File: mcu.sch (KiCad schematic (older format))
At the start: 71 parts, among them J10 JTAG, J11 esp32L, J12 esp32B, J13 esp32R, J2 SPI1, J3 uSD, J4 I2C1, J5 serial1, J6 serial2, J7 touch interface, J8 LCD 4.3, J9 EXT_IOS, Q1 ZXMN2F30FH, Q2 ZXMN2F30FH, Q3 ZXMN2F30FH, SW1 reset, U3 AT25SF641, U5 STM32F750Z8, U6 MP3302DJ-LF-P, U7 ESP32-WROOM-32, Y1 25MHz, Y2 32.768 kHz

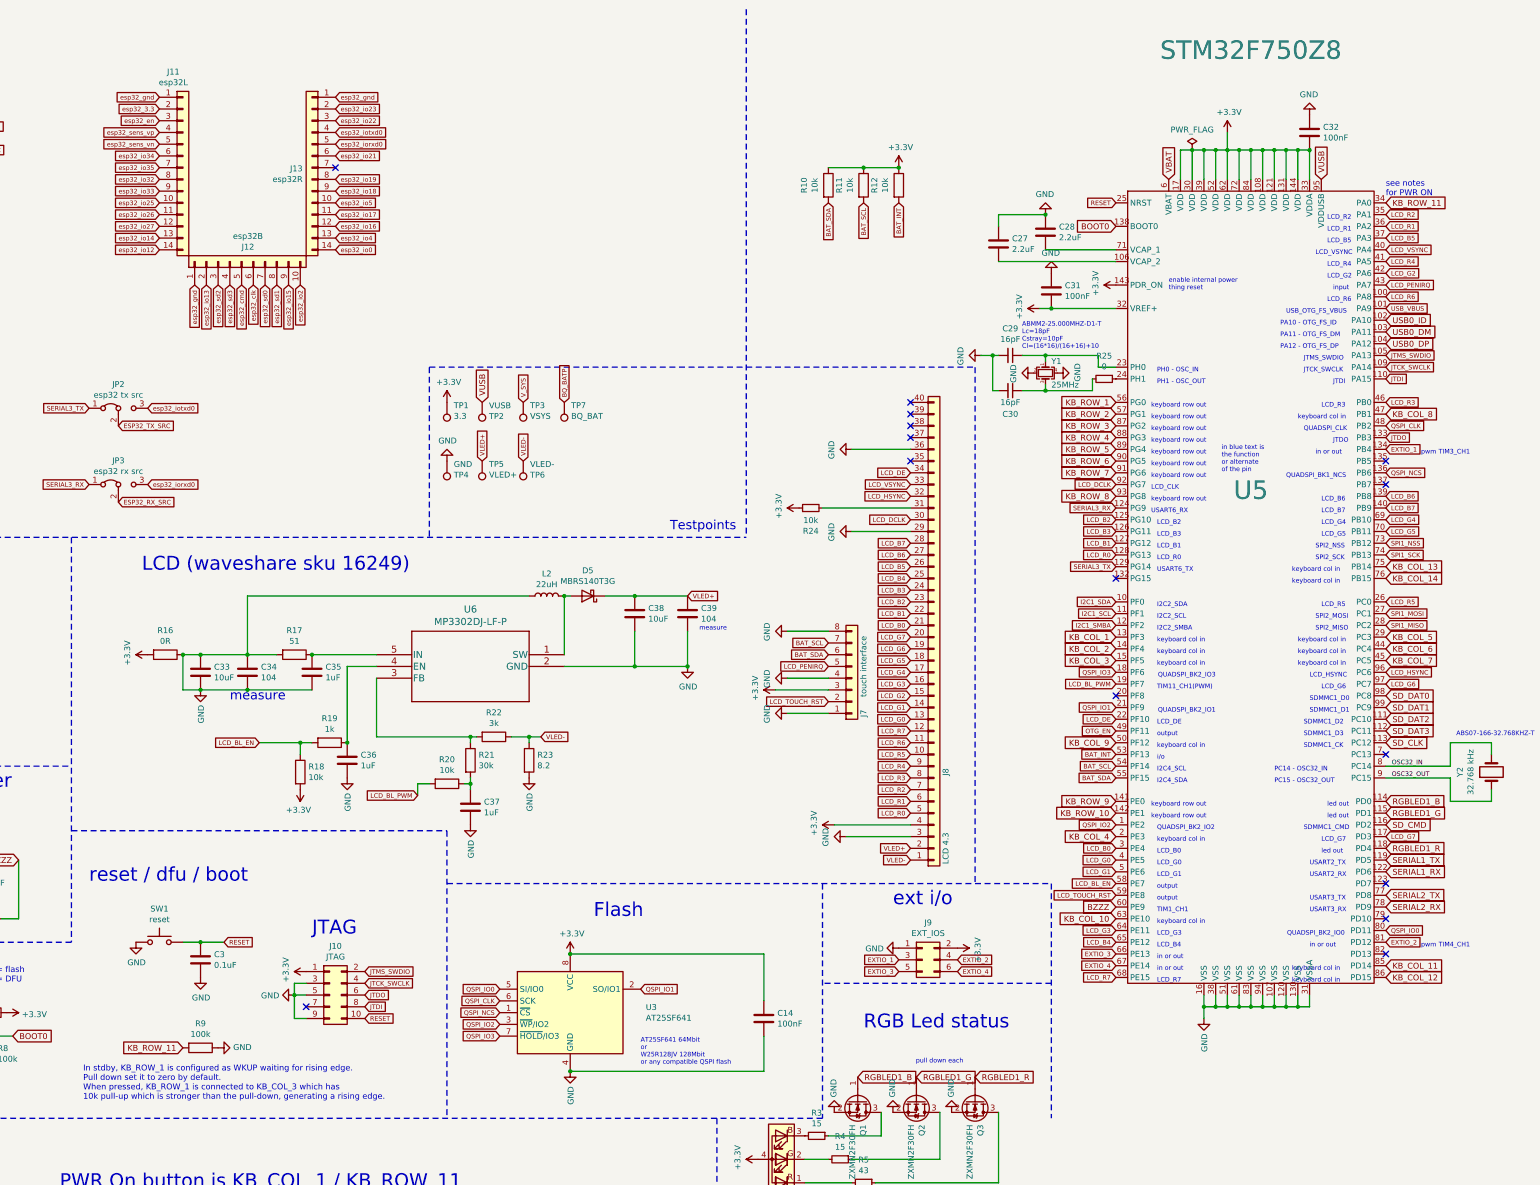
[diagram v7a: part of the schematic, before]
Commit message: Switch keyboard matrix input to a mcp23017
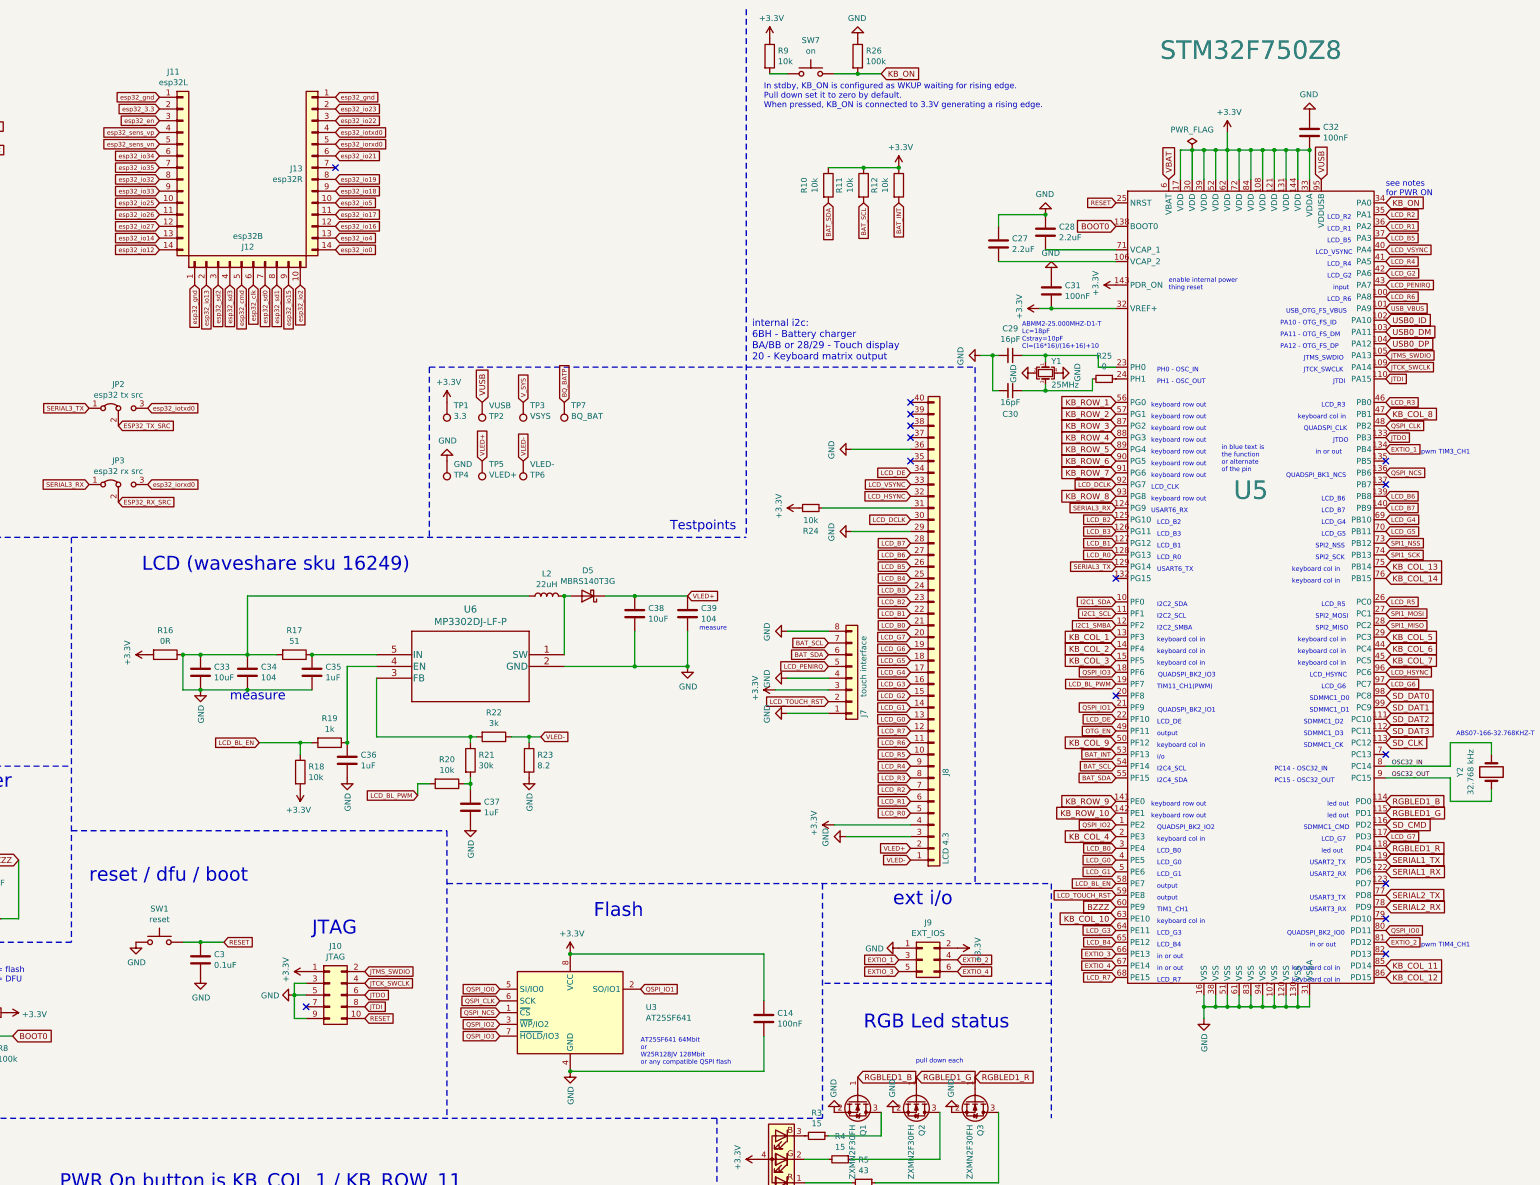
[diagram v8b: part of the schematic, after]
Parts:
- added R26: 100k, Resistor_SMD:R_0805_2012Metric_Pad1.20x1.40mm_HandSolder, symbol Device:R
- added SW7: on, Button_Switch_THT:SW_PUSH_6mm, symbol Switch:SW_Push
- R9: value 100k -> 10k
- U3: lcsc (none) -> C161772
- U5: lcsc (none) -> C411817
- U6: lcsc (none) -> C15035
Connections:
- net +3V3: now also R9.1
- net GND: now also R26.1; no longer R9.1
- net KB_ROW_11: no longer names the net of R9.2
- net KB_ROW_11: now also SW7.1; no longer U5.34 (PA0)
- new net KB_ON: R26.2, SW7.2, U5.34 (PA0)
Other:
- note added: "In stdby, KB_ON is configured as WKUP waiting for rising edge.\nPull down set it to zero by default.\nWhen pressed, KB_ON is connected to 3.3V generating a rising edge."
- note added: "internal i2c:\n6BH - Battery charger\nBA/BB or 28/29 - Touch display\n20 - Keyboard matrix output"
- note removed: "In stdby, KB_ROW_1 is configured as WKUP waiting for rising edge.\nPull down set it to zero by default.\nWhen pressed, KB_ROW_1 is connected to KB_COL_3 which has\n10k pull-up which is stronger than the pull-down, generating a rising edge."
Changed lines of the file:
@@
 F 2 "Package_SO:SOIC-8_3.9x4.9mm_P1.27mm" H 8100 8450 50  0001 C CNN
 F 3 "https://www.adestotech.com/wp-content/uploads/DS-AT25SF081_045.pdf" H 8100 9050 50  0001 C CNN
+F 4 "C161772" H 8100 9050 50  0001 C CNN "lcsc"
 	1    8100 9050
 	1    0    0    -1
@@
 KB_ROW_10
 Text GLabel 15050 2150 2    50   Input ~ 0
-KB_ROW_11
+KB_ON
 Text Notes 3750 10750 0    118  ~ 0
 PWR On button is KB_COL_1 / KB_ROW_11\nESC button is KB_COL_12 / KB_ROW_1
@@
 Text Notes 600  11100 0    98   ~ 0
 TODO to validate:\n- BOOT0 behavior\n- WAKEUP through ON behavior\n- RESET
-Text GLabel 4800 9350 0    50   Input ~ 0
-KB_ROW_11
-$Comp
-L Device:R R9
-U 1 1 5FF2A539
-P 4950 9350
-F 0 "R9" V 4743 9350 50  0000 C CNN
-F 1 "100k" V 4834 9350 50  0000 C CNN
-F 2 "Resistor_SMD:R_0805_2012Metric_Pad1.20x1.40mm_HandSolder" V 4880 9350 50  0001 C CNN
-F 3 "~" H 4950 9350 50  0001 C CNN
-	1    4950 9350
-	0    1    1    0
-$EndComp
-$Comp
-L power:GND #PWR0125
-U 1 1 5FF2B25B
-P 5100 9350
-F 0 "#PWR0125" H 5100 9100 50  0001 C CNN
-F 1 "GND" V 5105 9222 50  0000 R CNN
-F 2 "" H 5100 9350 50  0001 C CNN
-F 3 "" H 5100 9350 50  0001 C CNN
-	1    5100 9350
-	0    -1   -1   0
-$EndComp
-Text Notes 3950 9800 0    50   ~ 0
-In stdby, KB_ROW_1 is configured as WKUP waiting for rising edge.\nPull down set it to zero by default.\nWhen pressed, KB_ROW_1 is connected to KB_COL_3 which has\n10k pull-up which is stronger than the pull-down, generating a rising edge.
 Text Notes 15050 2100 0    50   ~ 0
 see notes\nfor PWR ON
@@
 F 2 "d_mps:MP3302DJ-LF-P" H 8850 6240 60  0001 C CNN
 F 3 "" H 8050 6000 60  0000 C CNN
+F 4 "C15035" H 8050 6000 50  0001 C CNN "lcsc"
 	1    8050 6000
 	-1   0    0    -1
@@
 F 2 "Package_QFP:LQFP-144_20x20mm_P0.5mm" H 13800 2200 157 0001 C CNN
 F 3 "" H 13800 2200 157 0001 C CNN
+F 4 "C411817" H 13900 2050 50  0001 C CNN "lcsc"
 	1    13900 2050
 	1    0    0    -1
@@
 Text Notes 10550 10900 0    39   ~ 0
 R VF=1.8-2.4 FC=30\nG VF=2.8-3.9 FC=20\nB VF=2.8-3.9 FC=20\nSupply=3.3
+Text GLabel 10750 1050 2    50   Input ~ 0
+KB_ON
+$Comp
+L Switch:SW_Push SW7
+U 1 1 5F9751F4
+P 10150 1050
+F 0 "SW7" H 10150 1335 50  0000 C CNN
+F 1 "on" H 10150 1244 50  0000 C CNN
+F 2 "Button_Switch_THT:SW_PUSH_6mm" H 10150 1250 50  0001 C CNN
+F 3 "~" H 10150 1250 50  0001 C CNN
+	1    10150 1050
+	1    0    0    -1
+$EndComp
+$Comp
+L Device:R R26
+U 1 1 5F97E218
+P 10550 900
+F 0 "R26" H 10620 946 50  0000 L CNN
+F 1 "100k" H 10620 855 50  0000 L CNN
+F 2 "Resistor_SMD:R_0805_2012Metric_Pad1.20x1.40mm_HandSolder" V 10480 900 50  0001 C CNN
+F 3 "~" H 10550 900 50  0001 C CNN
+	1    10550 900
+	1    0    0    -1
+$EndComp
+Wire Wire Line
+	10350 1050 10550 1050
+Connection ~ 10550 1050
+Wire Wire Line
+	10550 1050 10750 1050
+$Comp
+L power:GND #PWR0111
+U 1 1 5F98559E
+P 10550 750
+F 0 "#PWR0111" H 10550 500 50  0001 C CNN
+F 1 "GND" H 10555 577 50  0000 C CNN
+F 2 "" H 10550 750 50  0001 C CNN
+F 3 "" H 10550 750 50  0001 C CNN
+	1    10550 750
+	-1   0    0    1
+$EndComp
+$Comp
+L Device:R R9
+U 1 1 5F987D50
+P 9800 900
+F 0 "R9" H 9870 946 50  0000 L CNN
+F 1 "10k" H 9870 855 50  0000 L CNN
+F 2 "Resistor_SMD:R_0805_2012Metric_Pad1.20x1.40mm_HandSolder" V 9730 900 50  0001 C CNN
+F 3 "~" H 9800 900 50  0001 C CNN
+	1    9800 900
+	1    0    0    -1
+$EndComp
+Wire Wire Line
+	9800 1050 9950 1050
+$Comp
+L power:+3.3V #PWR0125
+U 1 1 5F98FA73
+P 9800 750
+F 0 "#PWR0125" H 9800 600 50  0001 C CNN
+F 1 "+3.3V" H 9815 923 50  0000 C CNN
+F 2 "" H 9800 750 50  0001 C CNN
+F 3 "" H 9800 750 50  0001 C CNN
+	1    9800 750
+	1    0    0    -1
+$EndComp
+Text Notes 9750 1350 0    50   ~ 0
+In stdby, KB_ON is configured as WKUP waiting for rising edge.\nPull down set it to zero by default.\nWhen pressed, KB_ON is connected to 3.3V generating a rising edge.
+Text Notes 9650 3500 0    59   ~ 0
+internal i2c:\n6BH - Battery charger\nBA/BB or 28/29 - Touch display\n20 - Keyboard matrix output
 $EndSCHEMATC
